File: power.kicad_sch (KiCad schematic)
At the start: 16 parts, among them U3 LM5166X, U5 TLV1117-33

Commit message: More schematic updates
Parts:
- added D26, D3: GREEN_LED, LED_SMD:LED_0603_1608Metric_Castellated, symbol Device:LED
- added R102, R103: 1k, Resistor_SMD:R_0402_1005Metric, symbol Device:R
- C41, C43, C44: footprint Capacitor_SMD:C_1206_3216Metric -> Capacitor_SMD:C_0402_1005Metric
- C42, C45, C46, C47, C48: footprint Capacitor_SMD:C_0805_2012Metric -> Capacitor_SMD:C_0402_1005Metric
- R4, R5, R6: footprint Resistor_SMD:R_0603_1608Metric_Pad0.98x0.95mm_HandSolder -> Resistor_SMD:R_0402_1005Metric
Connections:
- net +3V3: now also R103.1
- net +5V: now also R102.1
- net GND: now also D26.1 (K), D3.1 (K)
- new net: D3.2 (A), R102.2
- new net: D26.2 (A), R103.2
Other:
- moved on the sheet: C41, C42, C43, C44, C45, F1, L1, R4, R5, R6, U3

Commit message: Updated all of component values
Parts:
- C41, C43: footprint Capacitor_SMD:C_0402_1005Metric -> Capacitor_SMD:C_1206_3216Metric
- C42: footprint Capacitor_SMD:C_0402_1005Metric -> Capacitor_SMD:C_0805_2012Metric; Part Number C0805C333K5RACTU -> C0805C333K5RAC7800; Price ($) 0.12 -> 0.11
- C44: Comment 2.2µF ±10% 100V Ceramic Capacitor X7S 1206 (3216 Metric) -> 2.2 µF ±20% 16V Ceramic Capacitor X6S 0402 (1005 Metric); Digikey Number 587-5026-2-ND -> 490-10444-1-ND; Part Number HMK316AC7225KL-TE -> GRM155C81C225ME15D; Price ($) 0.53 -> 0.24
- C45, C48: Comment 0.1µF -20%, +80% 16V Ceramic Capacitor Y5V 0805 (2012 Metri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 -> 0.1 µF ±10% 16V Ceramic Capacitor X7R 0402 (1005 Metric); Digikey Number 399-9159-2-ND -> 311-1338-1-ND; Part Number C0805C104Z4VACTU -> CC0402KRX7R7BB104; Price ($) 0.11 -> 0.1
- C46, C47: footprint Capacitor_SMD:C_0402_1005Metric -> Capacitor_SMD:C_0805_2012Metric
- C49: Comment (none) -> 10000 pF ±10% 50V Ceramic Capacitor X7R 0402 (1005 Metric); Digikey Number (none) -> 490-4762-1-ND; Part Number (none) -> GCM155R71H103KA55D; Price ($) (none) -> 0.1
- L1: Price 0.85 -> (none); Price ($) (none) -> 0.85
- R102, R103: Comment (none) -> 1 kOhms ±1% 0.063W, 1/16W Chip Resistor 0402 (1005 Metric) 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; Digikey Number (none) -> 311-1.00KLRCT-ND; Part Number (none) -> RC0402FR-071KL; Price ($) (none) -> 0.1
- R4: Comment (none) -> 10 kOhms ±1% 0.063W, 1/16W Chip Resistor 0402 (1005 Metric)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; Digikey Number (none) -> 311-10.0KLRCT-ND; Part Number (none) -> RC0402FR-0710KL; Price ($) (none) -> 0.1
- R5: Comment (none) -> 71.5 kOhms ±1% 0.063W, 1/16W Chip Resistor 0402 (1005 Metri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; Digikey Number (none) -> YAG3222CT-ND; Part Number (none) -> RC0402FR-0771K5L; Price ($) (none) -> 0.1
- R6: Comment (none) -> 105 kOhms ±1% 0.063W, 1/16W Chip Resistor 0402 (1005 Metric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; Digikey Number (none) -> YAG2946CT-ND; Part Number (none) -> RC0402FR-07105KL; Price ($) (none) -> 0.1

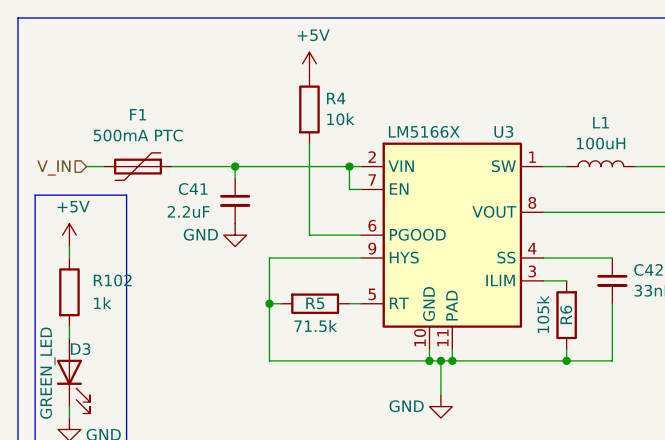
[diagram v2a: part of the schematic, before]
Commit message: DCDC Section Mostly complete
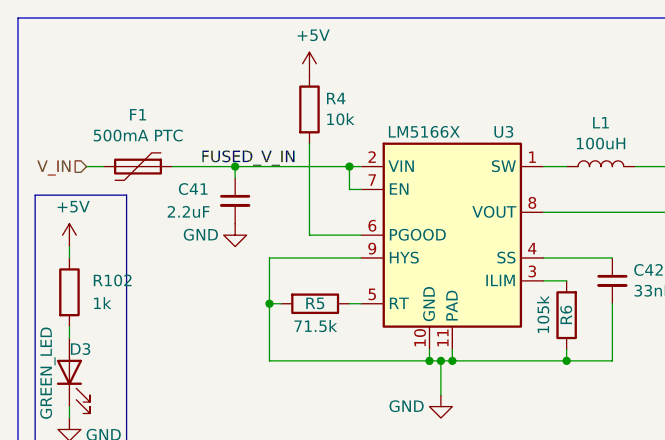
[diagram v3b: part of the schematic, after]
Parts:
- C42: footprint Capacitor_SMD:C_0805_2012Metric -> Capacitor_SMD:C_0402_1005Metric; Comment 0.033µF ±10% 50V Ceramic Capacitor X7R 0805 (2012 Metric) -> 3300 pF ±10% 50V Ceramic Capacitor X7R 0402 (1005 Metric); Digikey Number 399-1165-2-ND -> 311-1034-1-ND; Part Number C0805C333K5RAC7800 -> CC0402KRX7R9BB332; Price ($) 0.11 -> 0.1
- D26, D3: footprint LED_SMD:LED_0603_1608Metric_Castellated -> LED_SMD:LED_0603_1608Metric
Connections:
- net FUSED_V_IN: now reaches C41.1, F1.1, U3.2 (VIN), U3.7 (EN)
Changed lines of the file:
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@@
     (effects (font (size 1.27 1.27) italic) (justify right bottom))
+  )
+  (label "FUSED_V_IN" (at 34.29 30.48 0)
+    (effects (font (size 1.27 1.27)) (justify left bottom))
   )
   (hierarchical_label "V_IN" (shape input) (at 21.59 30.48 180)
@@
       (effects (font (size 1.27 1.27)) (justify right))
     )
-    (property "Footprint" "LED_SMD:LED_0603_1608Metric_Castellated" (id 2) (at 19.685 53.34 0)
+    (property "Footprint" "LED_SMD:LED_0603_1608Metric" (id 2) (at 19.685 53.34 0)
       (effects (font (size 1.27 1.27)) hide)
     )
@@
       (effects (font (size 1.27 1.27)) (justify left))
     )
-    (property "Footprint" "Capacitor_SMD:C_0805_2012Metric" (id 2) (at 80.01 43.18 0)
-      (effects (font (size 1.27 1.27)) hide)
-    )
-    (property "Datasheet" "https://content.kemet.com/datasheets/KEM_C1002_X7R_SMD.pdf" (id 3) (at 80.01 43.18 0)
-      (effects (font (size 1.27 1.27)) hide)
-    )
-    (property "Part Number" "C0805C333K5RAC7800" (id 4) (at 80.01 43.18 0)
-      (effects (font (size 1.27 1.27)) hide)
-    )
-    (property "Digikey Number" "399-1165-2-ND" (id 5) (at 80.01 43.18 0)
-      (effects (font (size 1.27 1.27)) hide)
-    )
-    (property "Price ($)" "0.11" (id 6) (at 80.01 43.18 0)
-      (effects (font (size 1.27 1.27)) hide)
-    )
-    (property "Comment" "0.033µF ±10% 50V Ceramic Capacitor X7R 0805 (2012 Metric)" (id 7) (at 80.01 43.18 0)
+    (property "Footprint" "Capacitor_SMD:C_0402_1005Metric" (id 2) (at 80.01 43.18 0)
+      (effects (font (size 1.27 1.27)) hide)
+    )
+    (property "Datasheet" "https://www.yageo.com/upload/media/product/productsearch/datasheet/mlcc/UPY-GPHC_X7R_6.3V-to-250V_22.pdf" (id 3) (at 80.01 43.18 0)
+      (effects (font (size 1.27 1.27)) hide)
+    )
+    (property "Part Number" "CC0402KRX7R9BB332" (id 4) (at 80.01 43.18 0)
+      (effects (font (size 1.27 1.27)) hide)
+    )
+    (property "Digikey Number" "311-1034-1-ND" (id 5) (at 80.01 43.18 0)
+      (effects (font (size 1.27 1.27)) hide)
+    )
+    (property "Price ($)" "0.1" (id 6) (at 80.01 43.18 0)
+      (effects (font (size 1.27 1.27)) hide)
+    )
+    (property "Comment" "3300 pF ±10% 50V Ceramic Capacitor X7R 0402 (1005 Metric)" (id 7) (at 80.01 43.18 0)
       (effects (font (size 1.27 1.27)) hide)
     )
@@
       (effects (font (size 1.27 1.27)) (justify right))
     )
-    (property "Footprint" "LED_SMD:LED_0603_1608Metric_Castellated" (id 2) (at 128.27 53.975 0)
-      (effects (font (size 1.27 1.27)) hide)
-    )
+    (property "Footprint" "LED_SMD:LED_0603_1608Metric" (id 2) (at 128.27 53.975 0)
+      (effects (font (size 1.27 1.27)) hide)
+    )
